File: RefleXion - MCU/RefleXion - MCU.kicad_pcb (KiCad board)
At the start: 2 copper layers, 94.3 x 28.8 mm, 20 parts, among them J1 Conn_01x21, J2 USB_C_Receptacle_USB2.0, J5 Conn_01x21, J6 USB_C_Receptacle_USB2.0, Q1 AO3401A, U1 WeAct_Blackpill_v3_safepin, U2 SRV05-4, U3 74AHCT1G125

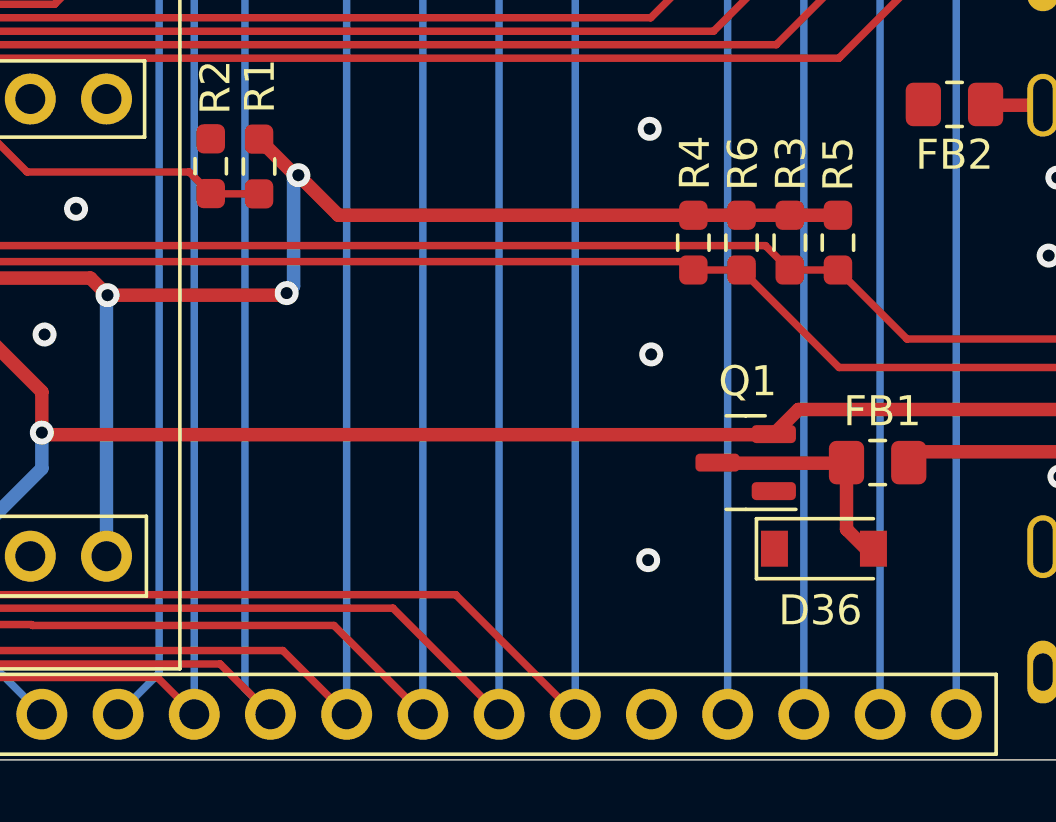
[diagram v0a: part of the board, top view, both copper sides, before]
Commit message: fixes to RGB
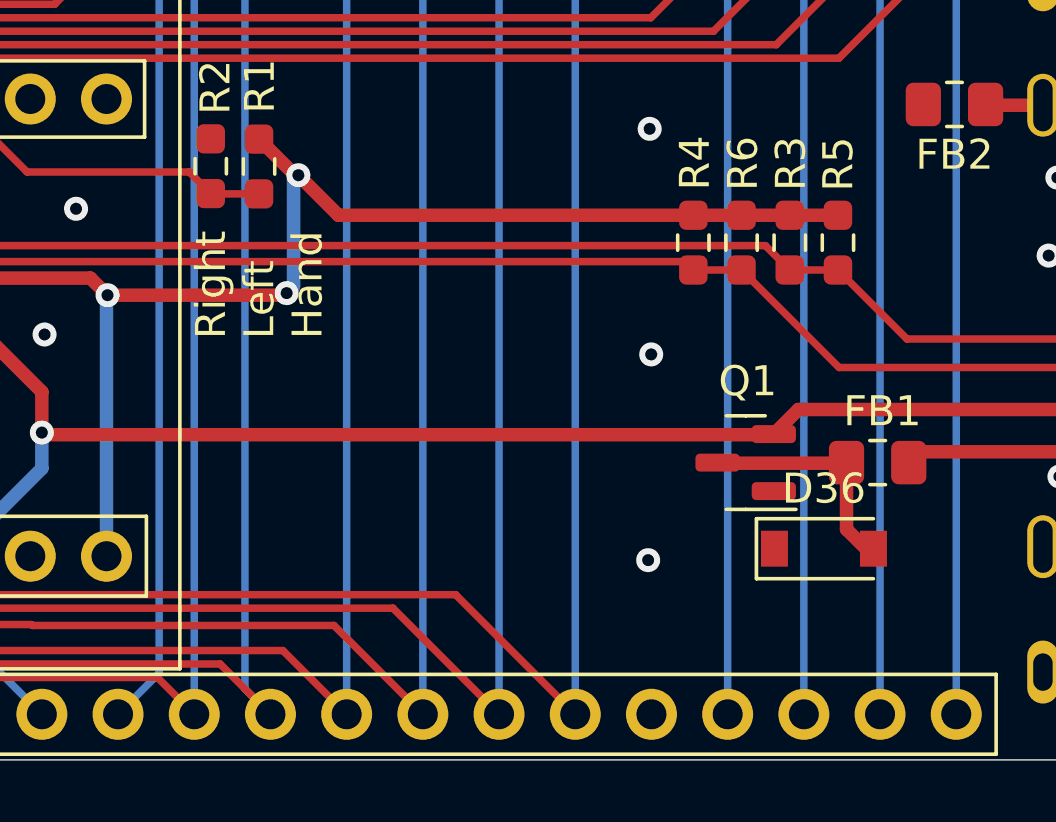
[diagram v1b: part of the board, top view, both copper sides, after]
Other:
- board text added: "Right Left Hand"
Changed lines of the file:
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@@
     (property "Sheetname" "")
     (attr smd)
-    (fp_text reference "D36" (at -0.1196 2.0576) (layer "F.SilkS")
+    (fp_text reference "D36" (at 0 -2) (layer "F.SilkS")
       (effects (font (size 1 1) (thickness 0.15)))
     )
@@
       (effects (font (size 1 1) (thickness 0.15)))
     )
-    (fp_line (start -2.25 -1) (end 1.65 -1) (layer "F.SilkS") (width 0.12))
     (fp_line (start -2.25 -1) (end -2.25 1) (layer "F.SilkS") (width 0.12))
+    (fp_line (start -2.25 -1) (end 1.65 -1) (layer "F.SilkS") (width 0.12))
     (fp_line (start -2.25 1) (end 1.65 1) (layer "F.SilkS") (width 0.12))
+    (fp_line (start -2.35 -1.15) (end -2.35 1.15) (layer "F.CrtYd") (width 0.05))
     (fp_line (start 2.35 -1.15) (end 2.35 1.15) (layer "F.CrtYd") (width 0.05))
-    (fp_line (start 2.35 1.15) (end -2.35 1.15) (layer "F.CrtYd") (width 0.05))
     (fp_line (start -2.35 -1.15) (end 2.35 -1.15) (layer "F.CrtYd") (width 0.05))
-    (fp_line (start -2.35 -1.15) (end -2.35 1.15) (layer "F.CrtYd") (width 0.05))
-    (fp_line (start -1.4 0.9) (end -1.4 -0.9) (layer "F.Fab") (width 0.1))
+    (fp_line (start 2.35 1.15) (end -2.35 1.15) (layer "F.CrtYd") (width 0.05))
+    (fp_line (start -0.75 0) (end -0.35 0) (layer "F.Fab") (width 0.1))
+    (fp_line (start 0.25 0) (end 0.75 0) (layer "F.Fab") (width 0.1))
     (fp_line (start -0.35 0) (end -0.35 0.55) (layer "F.Fab") (width 0.1))
-    (fp_line (start -0.35 0) (end 0.25 -0.4) (layer "F.Fab") (width 0.1))
+    (fp_line (start -1.4 0.9) (end -1.4 -0.9) (layer "F.Fab") (width 0.1))
     (fp_line (start 1.4 0.9) (end -1.4 0.9) (layer "F.Fab") (width 0.1))
-    (fp_line (start 0.25 0.4) (end -0.35 0) (layer "F.Fab") (width 0.1))
-    (fp_line (start -1.4 -0.9) (end 1.4 -0.9) (layer "F.Fab") (width 0.1))
-    (fp_line (start 0.25 0) (end 0.75 0) (layer "F.Fab") (width 0.1))
-    (fp_line (start -0.75 0) (end -0.35 0) (layer "F.Fab") (width 0.1))
-    (fp_line (start 1.4 -0.9) (end 1.4 0.9) (layer "F.Fab") (width 0.1))
     (fp_line (start -0.35 0) (end -0.35 -0.55) (layer "F.Fab") (width 0.1))
     (fp_line (start 0.25 -0.4) (end 0.25 0.4) (layer "F.Fab") (width 0.1))
+    (fp_line (start -1.4 -0.9) (end 1.4 -0.9) (layer "F.Fab") (width 0.1))
+    (fp_line (start -0.35 0) (end 0.25 -0.4) (layer "F.Fab") (width 0.1))
+    (fp_line (start 1.4 -0.9) (end 1.4 0.9) (layer "F.Fab") (width 0.1))
+    (fp_line (start 0.25 0.4) (end -0.35 0) (layer "F.Fab") (width 0.1))
     (pad "1" smd rect (at -1.65 0) (size 0.9 1.2) (layers "F.Cu" "F.Paste" "F.Mask")
       (net 29 "GND") (pinfunction "A1") (pintype "passive"))
@@
     (effects (font (size 1 1) (thickness 0.15)))
   )
+  (gr_text "Right\nLeft\nHand" (at 100.07 51.76 90) (layer "F.SilkS")
+    (effects (font (size 1 1) (thickness 0.15)) (justify left))
+  )
   (segment (start 56.875 59) (end 58.056497 57.818503) (width 0.25) (layer "F.Cu") (net 1))

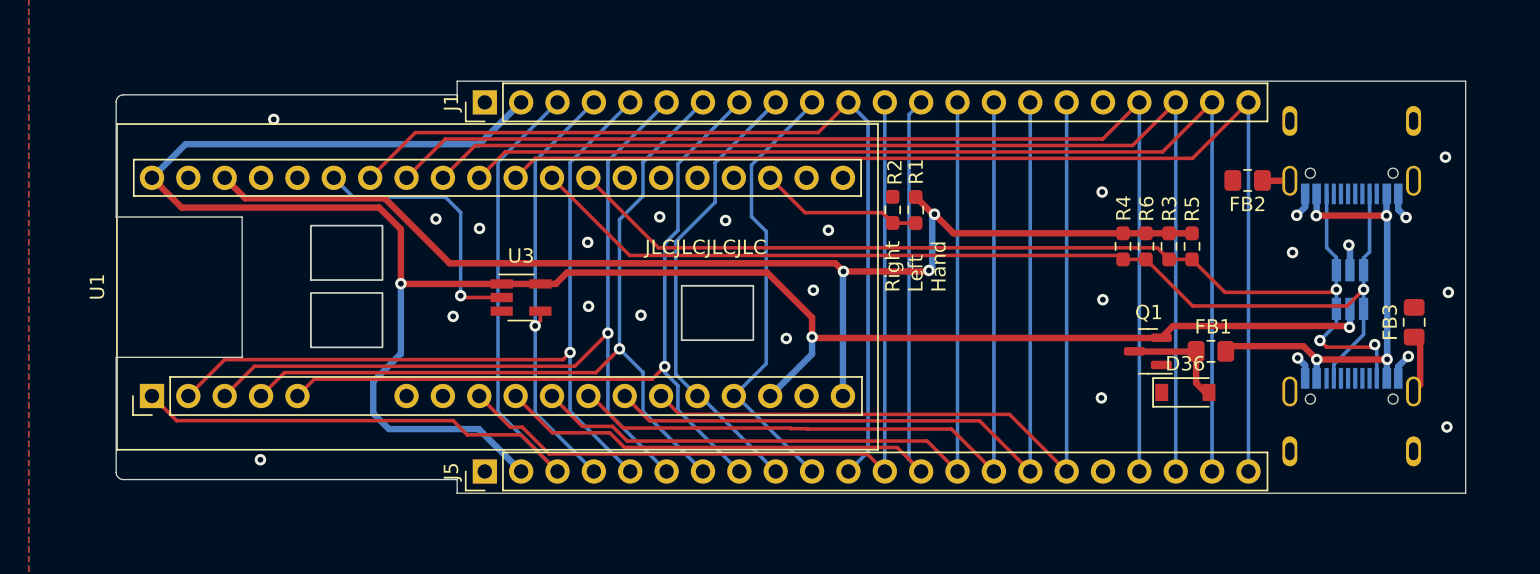
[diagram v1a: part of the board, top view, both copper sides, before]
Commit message: updated for RGB
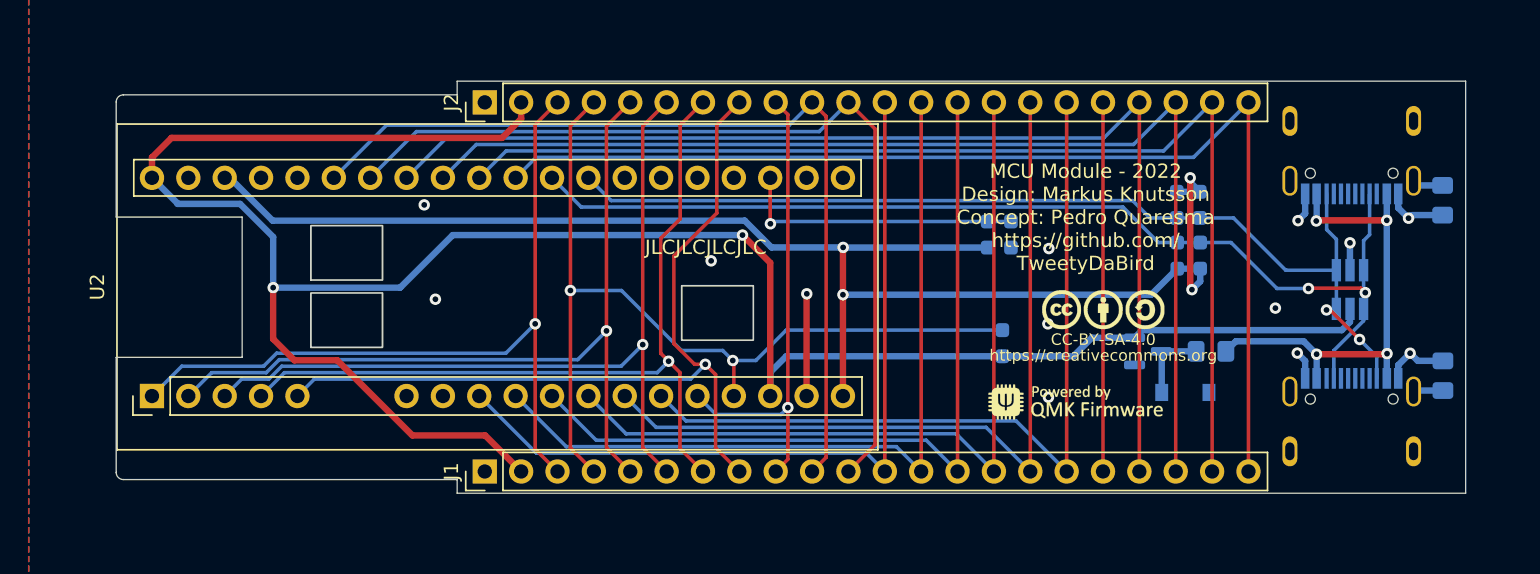
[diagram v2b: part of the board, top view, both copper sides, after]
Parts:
- removed U3: 74AHCT1G125, Package_TO_SOT_SMD:SOT-23-5_HandSoldering
- added R7: 4.7k, Resistor_SMD:R_0603_1608Metric_Pad0.98x0.95mm_HandSolder, B.Cu at (106.1, 55.3)
- D1: renamed from D36; moved to B.Cu
- FB1, Q1, R1, R2, R3, R4, R5, R6: moved to B.Cu
- FB2: renamed from FB3; moved to B.Cu
- FB3: renamed from FB2; moved to B.Cu
- Logo1, Logo2: moved to F.Cu
- moved FB3 13.7 mm to (136.9, 45.3), turned to -90 degrees
- moved Logo2 12.0 mm to (111.2, 59.4), turned to 0 degrees
- moved R2 8.44 mm to (106.7, 47.7), turned to -90 degrees
- moved R1 5.30 mm to (105.1, 47.7), turned to 90 degrees
- moved FB2 4.24 mm to (136.9, 57.6)
- moved R4 3.84 mm to (118.3, 49.2), turned to 90 degrees
- moved R6 3.84 mm to (119.9, 49.2), turned to 90 degrees
- moved R3 3.61 mm to (119.9, 45.6)
- moved Logo1 3.60 mm to (113.2, 53.9), turned to 0 degrees
- moved R5 3.09 mm to (118.3, 45.6)
- turned D1 to 180 degrees
- turned Q1 to 0 degrees
- renumbered J5 to J1, J1 to J2, J6 to J5, J2 to J6, U2 to U1, U1 to U2
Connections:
- J1 pad 4: RGB_OUT -> RGB
- J2 pad 4: RGB_OUT -> RGB
- J5 pad S2: (no net) -> Net-(FB2-Pad1)
- J5 pad S3: (no net) -> Net-(FB2-Pad1)
- J5 pad S4: (no net) -> Net-(FB2-Pad1)
- J6 pad S2: (no net) -> Net-(FB2-Pad1)
- J6 pad S3: (no net) -> Net-(FB2-Pad1)
- J6 pad S4: (no net) -> Net-(FB2-Pad1)
- U2 pad 17: B2 -> RGB
- U2 pad 35: RGB -> B2
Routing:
- net RGB: track 18.6 -> 62.7 mm, vias 1 -> 2
- net B2: track 31.3 -> 62.2 mm
- net RGB_OUT: track 30.4 -> 0.00 mm, vias 1 -> 0
- net unconnected-(J1-Pad18): track 0.00 -> 25.8 mm
- net +3.3V: track 85.1 -> 103.8 mm, vias 3 -> 4
- net GND: track 8.87 -> 22.2 mm, vias 25 -> 13
- net VCC: track 148.8 -> 158.8 mm, vias 3 -> 2
- net Hand: track 11.5 -> 20.1 mm, vias 0 -> 1
- net Col0: track 59.7 -> 55.9 mm, vias 0 -> 1
- net TX: track 73.2 -> 70.3 mm, vias 3 -> 2
- net Row0: track 56.6 -> 59.4 mm
- net /VBUS2: track 7.45 -> 5.30 mm
- net A2: track 31.7 -> 33.5 mm, vias 0 -> 1
- net Net-(FB2-Pad1): track 6.08 -> 4.24 mm
- net Col1: track 57.2 -> 58.2 mm
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
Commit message: big dump
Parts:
- removed the FB2 at (136.9, 57.6)
- removed R4, R5, R6: 9.1k, Resistor_SMD:R_0603_1608Metric_Pad0.98x0.95mm_HandSolder
- removed R7: 4.7k, Resistor_SMD:R_0603_1608Metric_Pad0.98x0.95mm_HandSolder
- Logo1, Logo2: moved to B.Cu
- moved R1 21.5 mm to (100.7, 55.2), turned to 90 degrees
- moved Logo2 7.11 mm to (108.8, 52.7), turned to 180 degrees
- moved FB2 6.18 mm to (135.9, 51.4), turned to 180 degrees
- moved Logo1 6.13 mm to (109.3, 58.6), turned to 180 degrees
- moved R3 4.54 mm to (100.8, 46.1)
- moved R2 4.02 mm to (103.0, 46.1)
- moved D1 2.56 mm to (121.5, 58.6)
- moved FB1 2.41 mm to (123.0, 55.5)
- moved Q1 2.30 mm to (118.5, 55.4)
- renumbered FB3 to FB2, J5 to J3, J6 to J4, R3 to R1, R1 to R3
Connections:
- FB2 pad 1: Net-(FB2-Pad1) -> GND
- FB2 pad 2: GND -> /SHIELD
- J3 pad A8: RX -> TX
- J3 pad B8: TX -> RX
- J3 pad S1: Net-(FB2-Pad1) -> /SHIELD
- J3 pad S2: Net-(FB2-Pad1) -> (no net)
- J4 pad S1: Net-(FB2-Pad1) -> /SHIELD
- J4 pad S2: Net-(FB2-Pad1) -> (no net)
- R1 pad 1: +3.3V -> VCC
- R1 pad 2: TX -> RGB
- U2 pad 17: RGB -> B2
- U2 pad 35: B2 -> RGB
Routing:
- net +3.3V: track 103.8 -> 63.4 mm, vias 4 -> 3
- net B2: track 62.2 -> 30.4 mm
- net VCC: track 158.8 -> 140.8 mm, vias 2 -> 3
- net /SHIELD: track 0.00 -> 16.6 mm
- net RGB: track 62.7 -> 79.1 mm, vias 2 -> 1
- net GND: track 22.2 -> 10.9 mm, vias 13 -> 17
- net Hand: track 20.1 -> 14.3 mm, vias 1 -> 0
- net Net-(FB2-Pad1): track 4.24 -> 0.00 mm
- net Col1: track 58.2 -> 62.3 mm, vias 1 -> 0
- net Col0: track 55.9 -> 59.8 mm, vias 1 -> 0
- net TX: track 70.3 -> 67.6 mm
- net /VBUS2: track 5.30 -> 7.90 mm
- net Row0: track 59.4 -> 56.9 mm
- net /VBUS1: track 33.4 -> 34.9 mm, vias 4 -> 3
- net A2: track 33.5 -> 32.2 mm, vias 1 -> 0
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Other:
- board text added: "LH"
- board text added: "MCU Module v1.1.0 - 2022 Design: Markus Knutsson Concept: Pedro Quaresma https://github.com/ TweetyDaBird"
- board text added: "RH"
- board text removed: "MCU Module - 2022 Design: Markus Knutsson Concept: Pedro Quaresma https://github.com/ TweetyDaBird"
- board text removed: "Right Left Hand"
